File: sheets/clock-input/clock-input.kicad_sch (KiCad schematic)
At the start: 5 parts, among them U1 40106

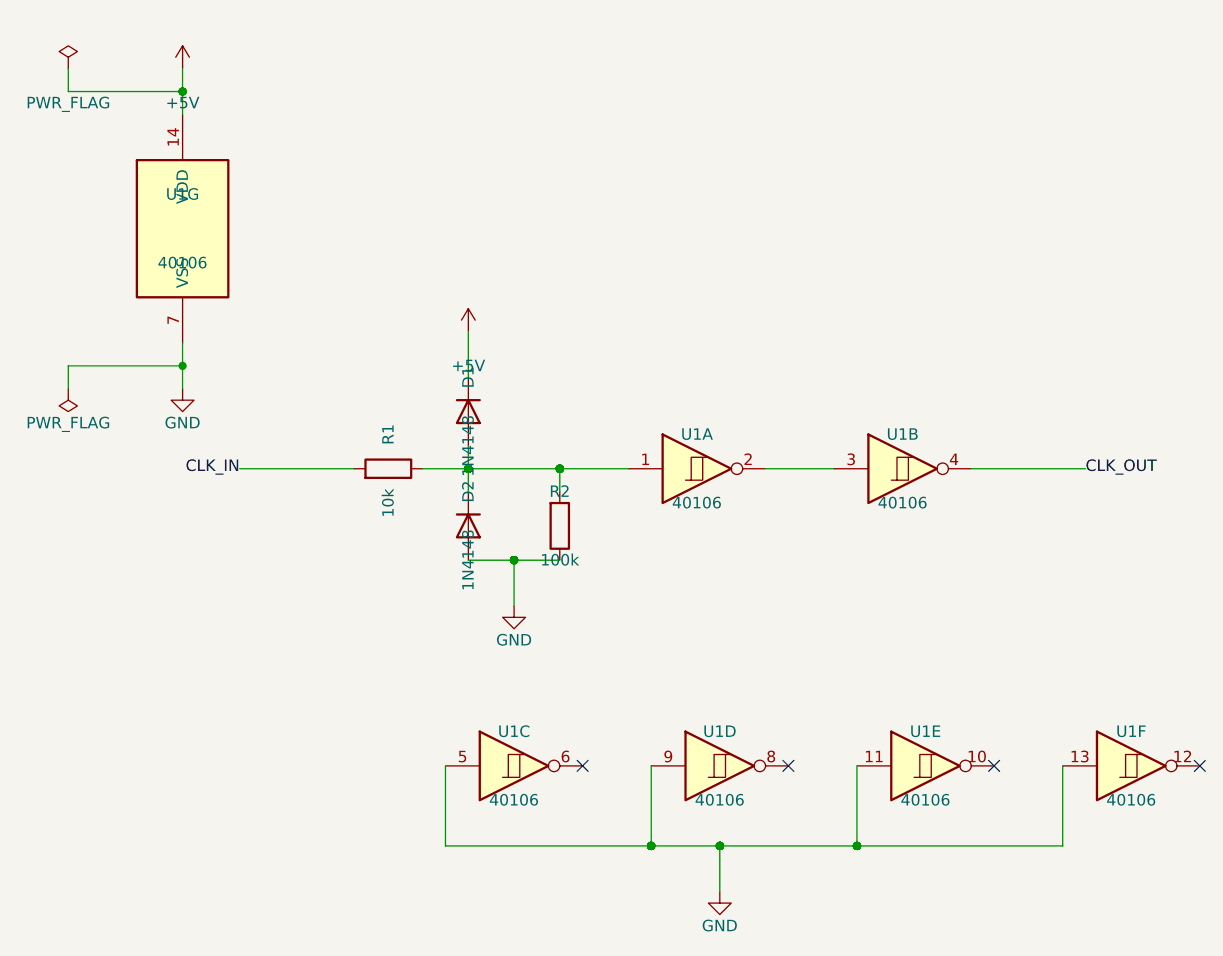
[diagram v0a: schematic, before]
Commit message: Tidy clock-input layout
Visual changes only, made in Eeschema. ERC unchanged at 0 errors.
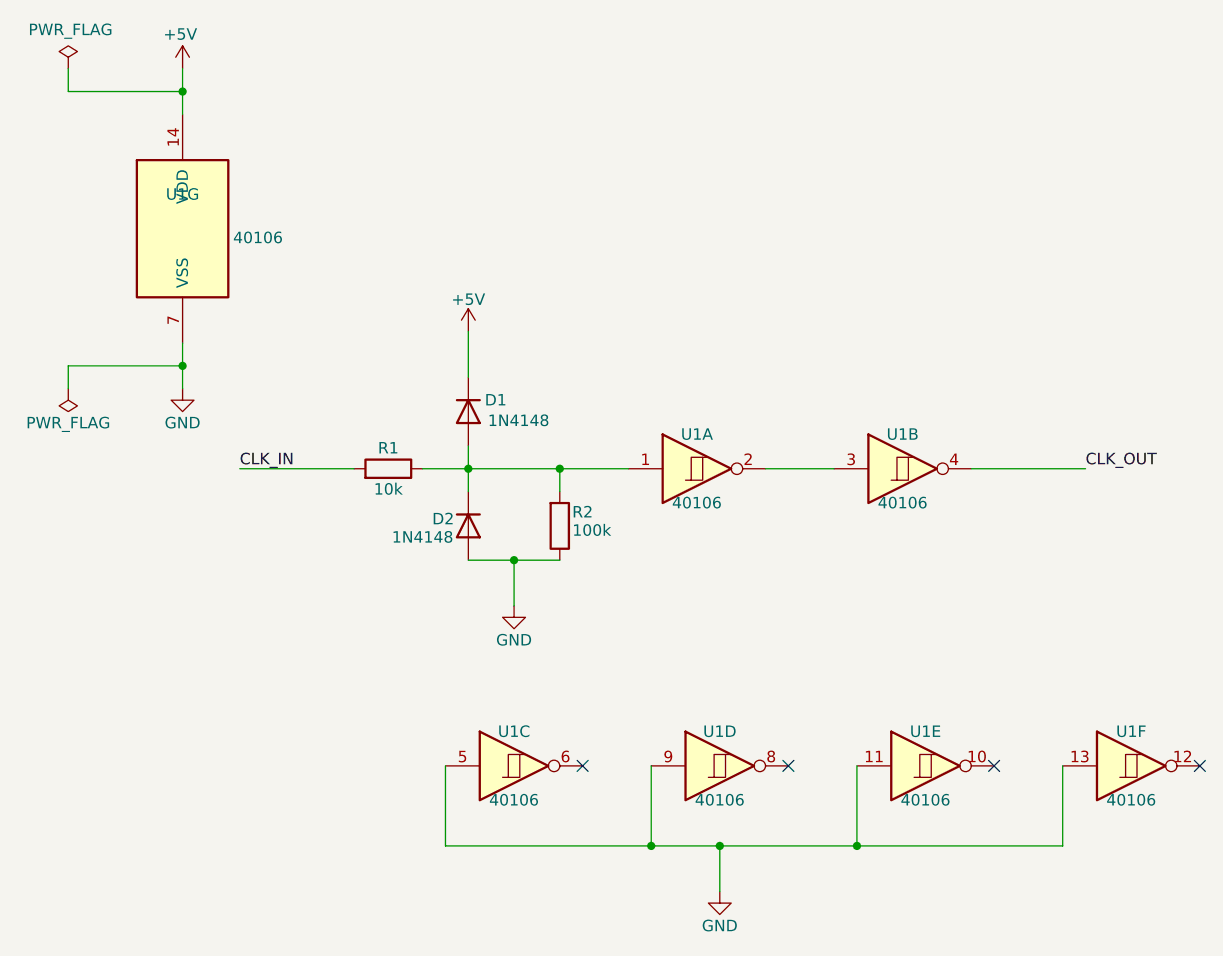
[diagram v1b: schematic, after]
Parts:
- U1: footprint Eurorack Common:DIP-14_W7.62mm -> (none)
